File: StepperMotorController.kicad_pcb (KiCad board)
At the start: 4 copper layers, 80 x 100 mm, 66 parts, among them J1 Conn_01x04, J2 Conn_01x04, J3 Conn_01x08, J4 Conn_01x02, J5 TC2070, M1 Mounting_Hole, M2 Mounting_Hole, M3 Mounting_Hole, M4 Mounting_Hole, U1 ACS725xLCTR-10AU, U10 SIR5802DP, U11 TMC5160A-TA, U12 STM32U575RGTx, U13 MCP2562-H-SN, U14 AP62300TWU, U2 AP62300TWU, U3 SIR5802DP, U4 SIR5802DP, U5 SIR5802DP, U6 SIR5802DP, U7 SIR5802DP, U8 SIR5802DP, U9 SIR5802DP

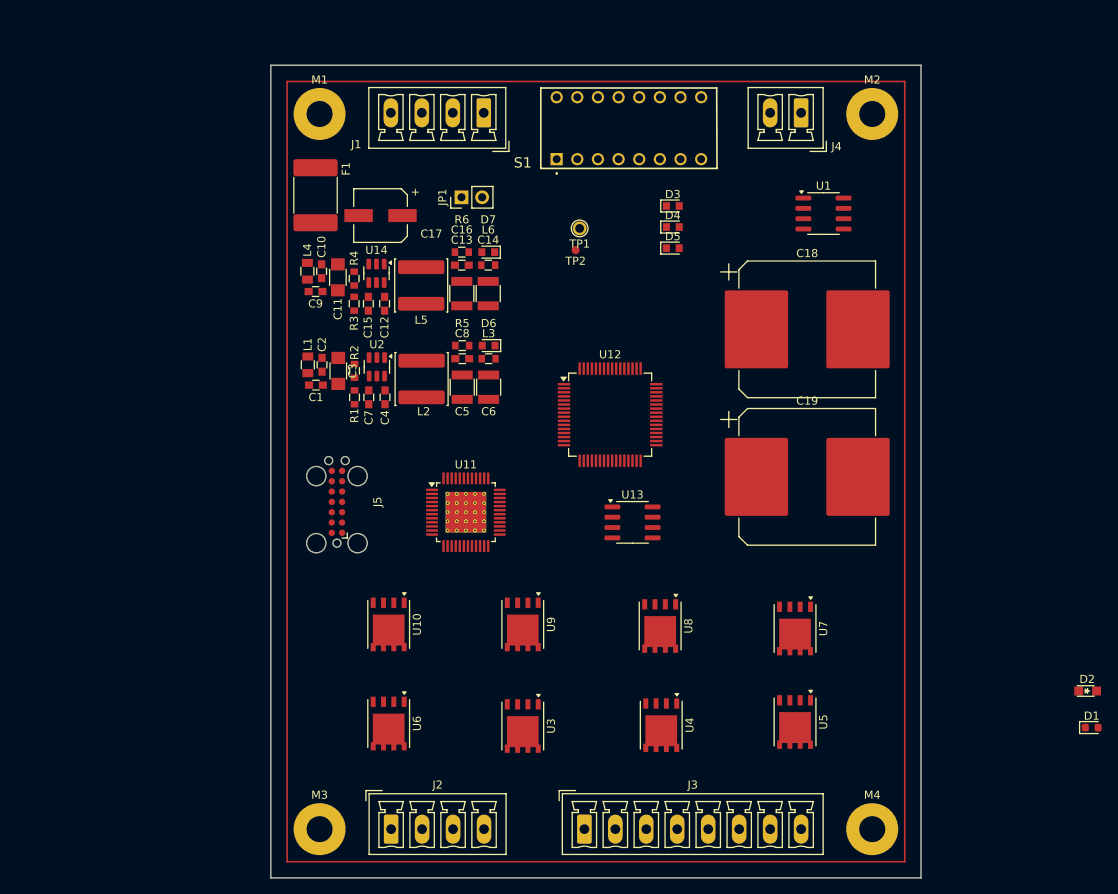
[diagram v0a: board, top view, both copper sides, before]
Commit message: PCB 3mm free space around edges, 9pin dipswitch, re-arragnged components
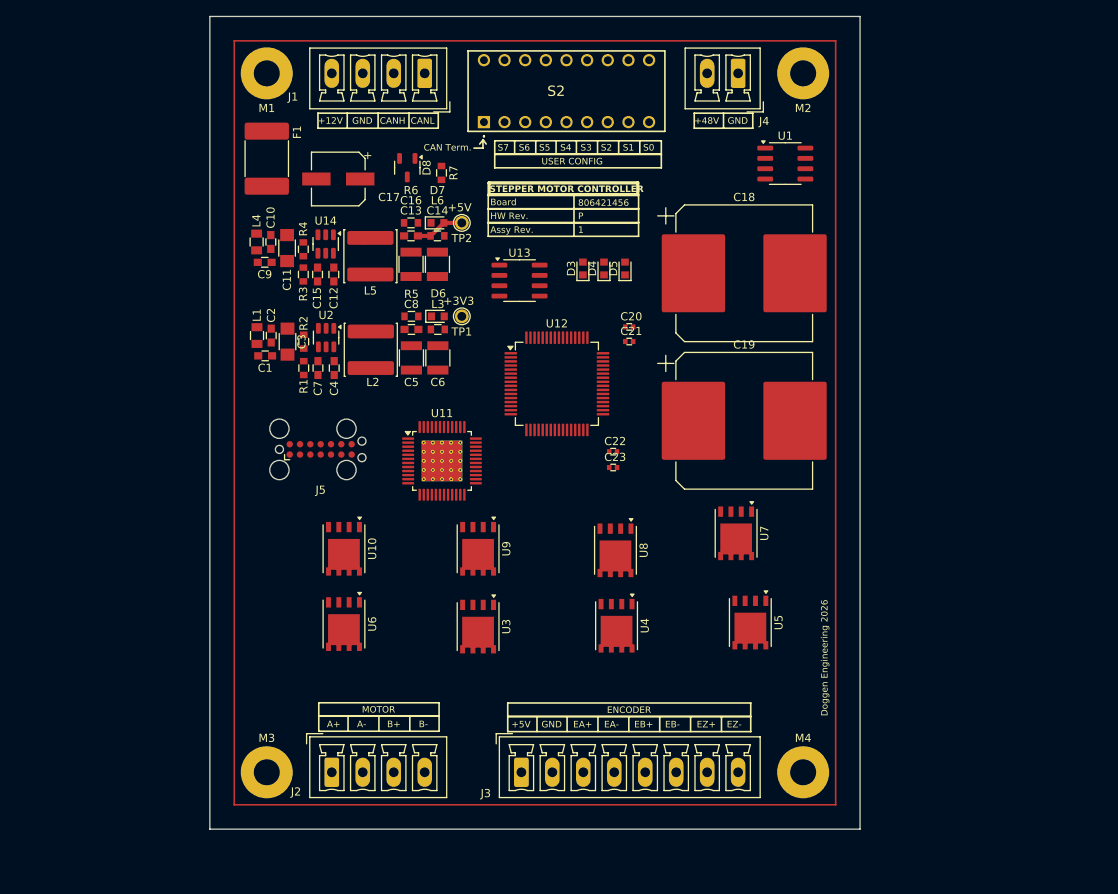
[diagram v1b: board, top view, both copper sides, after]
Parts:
- removed D1: LED, LED_SMD:LED_0603_1608Metric
- removed D2: LED0805BLUE#0805LED, D&R_Discrete:LED_0805
- removed JP1: Jumper_2_Open, Connector_PinHeader_2.54mm:PinHeader_1x02_P2.54mm_Vertical
- removed S1: MCNDS-08V, Doggen:MCNDS08V
- added C20: 100N-X7R_25V#0402, D&R_Passive:C_0402, F.Cu at (131.6, 58.2)
- added C21: 100N-X7R_25V#0402, D&R_Passive:C_0402, F.Cu at (131.6, 60.0)
- added C22: 100N-X7R_25V#0402, D&R_Passive:C_0402, F.Cu at (129.6, 73.5)
- added C23: 100N-X7R_25V#0402, D&R_Passive:C_0402, F.Cu at (129.6, 75.5)
- added D8: TPSM24CANB-02HTG, Package_TO_SOT_SMD:SOT-23-3, F.Cu at (104.3, 38.6)
- added R7: 120R#0603, D&R_Passive:R_0603, F.Cu at (108.5, 39.2)
- added S2: MCNDS-09V, Doggen:MCNDS09V, F.Cu at (113.7, 33.0)
- TP2: value Testpin -> Testpin_via; footprint D&R_Other:TP1mm -> D&R_Other:Testpoint_Via
- moved U13 32.8 mm to (118.1, 52.5)
- moved TP1 18.1 mm to (111.0, 56.9)
- moved TP2 14.4 mm to (111.0, 45.4)
- moved U7 13.8 mm to (144.8, 83.6)
- moved D3 13.5 mm to (125.9, 51.0), turned to 90 degrees
- moved U3 13.4 mm to (113.0, 95.1)
- moved U4 13.4 mm to (130.0, 95.0)
- moved U5 13.4 mm to (146.5, 94.6)
- moved U6 13.4 mm to (96.5, 94.8)
- moved M4 11.0 mm to (153.0, 113.0)
- moved U10 10.8 mm to (96.5, 85.5)
- moved U8 10.8 mm to (129.9, 85.7)
- moved U9 10.8 mm to (113.0, 85.5)
- moved J3 10.4 mm to (118.3, 113.0)
- moved C19 10.4 mm to (145.8, 69.8)
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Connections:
- J1 pad 1: GND -> Net-(J1-Pin_1)
- J1 pad 2: +12V -> Net-(J1-Pin_2)
- J1 pad 3: unconnected-(J1-Pin_3-Pad3) -> GND
- J1 pad 4: unconnected-(J1-Pin_4-Pad4) -> +12V
- TP1 pad 1: unconnected-(TP1-Pad1) -> +3V3
- TP2 pad 1: unconnected-(TP2-Pad1) -> +5V
- U12 pad 19: unconnected-(U12-VDD-Pad19) -> +3V3
- U12 pad 32: unconnected-(U12-VDD-Pad32) -> +3V3
- U12 pad 64: unconnected-(U12-VDD-Pad64) -> +3V3
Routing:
- net +5V: track 0.00 -> 6.06 mm
- net Net-(U14-SW): track 0.00 -> 1.06 mm
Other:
- board text added: "+12V"
- board text added: "+3V3"
- board text added: "+48V"
- board text added: "+5V"
- board text added: "1"
- board text added: "806421456"
- board text added: "A+"
- board text added: "A-"
- board text added: "Assy Rev."
- board text added: "B+"
- board text added: "B-"
- board text added: "Board"
- board text added: "CAN Term."
- board text added: "CANH"
- board text added: "CANL"
- board text added: "Doggen Engineering 2026"
- board text added: "EA+"
- board text added: "EA-"
- board text added: "EB+"
- board text added: "EB-"
- board text added: "ENCODER"
- board text added: "EZ+"
- board text added: "EZ-"
- board text added: "GND"
- board text added: "HW Rev."
- board text added: "MOTOR"
- board text added: "P"
- board text added: "S0"
- board text added: "S1"
- board text added: "S2"
- board text added: "S3"
- board text added: "S4"
- board text added: "S5"
- board text added: "S6"
- board text added: "S7"
- board text added: "STEPPER MOTOR CONTROLLER"
- board text added: "USER CONFIG"

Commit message: updated hierarchical sheets
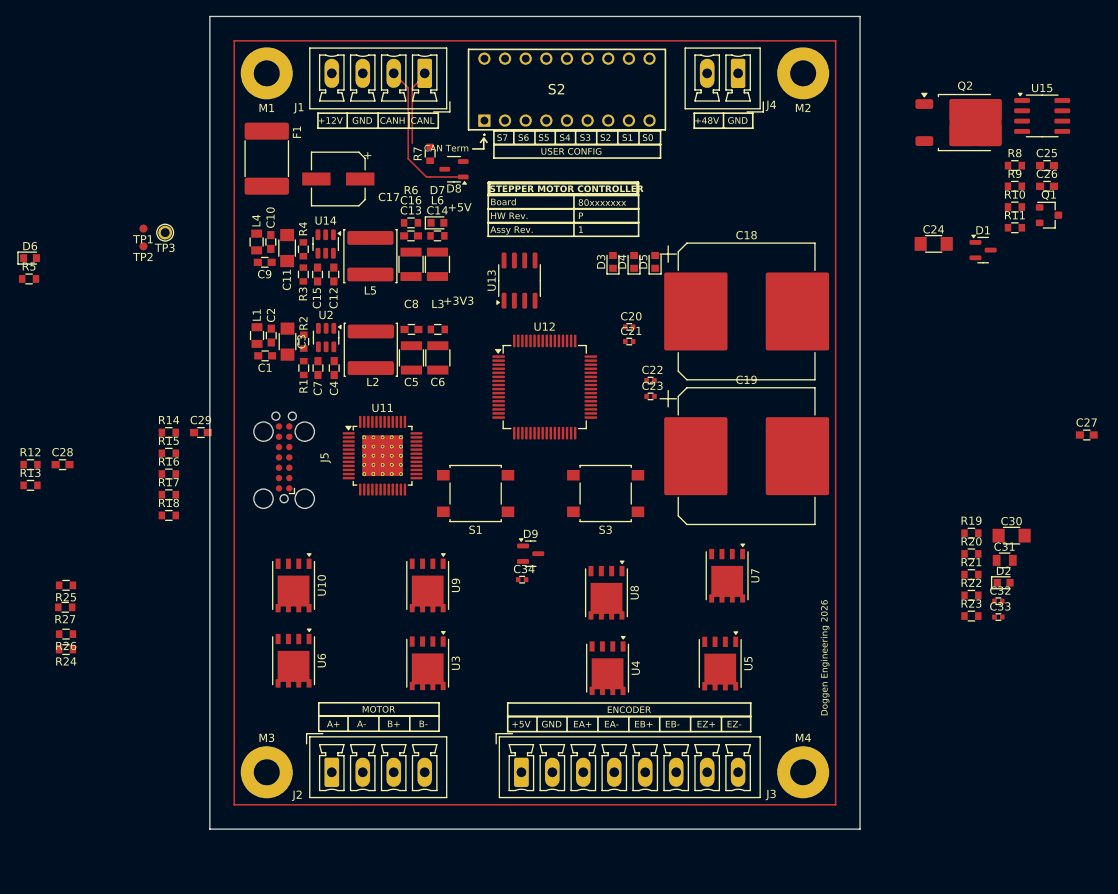
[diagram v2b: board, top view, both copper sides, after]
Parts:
- removed U1: ACS725xLCTR-10AU, Package_SO:SOIC-8_3.9x4.9mm_P1.27mm
- added C24: 10U-X5R_50V#1206, D&R_Passive:C_1206, F.Cu at (169.1, 48.0)
- added C25: 100N-X7R_50V#0603, D&R_Passive:C_0603, F.Cu at (183.0, 38.4)
- added C26: 1N-NP0_100V#0603, D&R_Passive:C_0603, F.Cu at (183.0, 40.9)
- added C27: 100N-X7R_100V#0603, D&R_Passive:C_0603, F.Cu at (187.9, 71.5)
- added C28: 100N-X7R_50V#0603, D&R_Passive:C_0603, F.Cu at (61.9, 75.2)
- added C29: 33P-NP0_50V#0603, D&R_Passive:C_0603, F.Cu at (78.9, 71.2)
- added C30: 4U7-X7R_25V#1206, D&R_Passive:C_1206, F.Cu at (178.7, 83.9)
- added C31: 1U-X7R_10V#0805, D&R_Passive:C_0805, F.Cu at (177.8, 86.9)
- added C32: 100N-X7R_25V#0402, D&R_Passive:C_0402, F.Cu at (177.0, 92.0)
- added C33: 100N-X7R_25V#0402, D&R_Passive:C_0402, F.Cu at (177.0, 93.9)
- added C34: 100N-X7R_25V#0402, D&R_Passive:C_0402, F.Cu at (118.4, 89.3)
- added D1: BZX84C15, Package_TO_SOT_SMD:SOT-23, F.Cu at (175.1, 48.8)
- added D2: LED0603BLUE_APT1608LVBC/D, D&R_Discrete:LED_0603_1608Metric, F.Cu at (177.7, 89.7)
- added D9: BAT54C, Package_TO_SOT_SMD:SOT-23, F.Cu at (119.5, 86.1)
- added Q1: BC807-25LT1#SOT23, D&R_Discrete:SOT-23, F.Cu at (183.2, 44.5)
- added Q2: MDT40P10D, Package_TO_SOT_SMD:TO-252-2, F.Cu at (172.9, 33.1)
- added R10: 56K#0603, D&R_Passive:R_0603, F.Cu at (179.1, 43.5)
- added R11: 1K#0603, D&R_Passive:R_0603, F.Cu at (179.1, 46.0)
- added R12: 10K#0603, D&R_Passive:R_0603, F.Cu at (57.9, 75.2)
- added R13: 10K#0603, D&R_Passive:R_0603, F.Cu at (57.9, 77.7)
- added R14: 100R#0603, D&R_Passive:R_0603, F.Cu at (75.0, 71.2)
- added R15: 100R#0603, D&R_Passive:R_0603, F.Cu at (75.0, 73.8)
- added R16: 100R#0603, D&R_Passive:R_0603, F.Cu at (75.0, 76.3)
- added R17: 10K#0603, D&R_Passive:R_0603, F.Cu at (75.0, 78.8)
- added R18: 100R#0603, D&R_Passive:R_0603, F.Cu at (75.0, 81.4)
- added R19: 3K3#0603, D&R_Passive:R_0603, F.Cu at (173.7, 83.6)
- added R20: 3K3#0603, D&R_Passive:R_0603, F.Cu at (173.7, 86.1)
- added R21: 3K3#0603, D&R_Passive:R_0603, F.Cu at (173.7, 88.7)
- added R22: 1K#0603, D&R_Passive:R_0603, F.Cu at (173.7, 91.2)
- added R23: 10R#0603, D&R_Passive:R_0603, F.Cu at (173.7, 93.8)
- added R24: 47R#0603, D&R_Passive:R_0603, F.Cu at (62.3, 97.9)
- added R25: 47R#0603, D&R_Passive:R_0603, F.Cu at (62.3, 90.0)
- added R26: 47R#0603, D&R_Passive:R_0603, F.Cu at (62.3, 96.0)
- added R27: 47R#0603, D&R_Passive:R_0603, F.Cu at (62.2, 92.7)
- added R8: 100R#0603, D&R_Passive:R_0603, F.Cu at (179.1, 38.4)
- added R9: 100K#0603, D&R_Passive:R_0603, F.Cu at (179.1, 40.9)
- added S1: Wurth_Tactile_Switch_430182043816, Button_Switch_SMD:SW_SPST_B3S-1000, F.Cu at (112.7, 78.7)
- added S3: Wurth_Tactile_Switch_430182043816, Button_Switch_SMD:SW_SPST_B3S-1000, F.Cu at (128.7, 78.7)
- added TP3: Testpin_via, D&R_Other:Testpoint_Via, F.Cu at (74.5, 46.6)
- added U15: ACS725xLCTR-30AB, Package_SO:SOIC-8_3.9x4.9mm_P1.27mm, F.Cu at (182.4, 32.2)
- TP1, TP2: value Testpin_via -> Testpin; footprint D&R_Other:Testpoint_Via -> D&R_Other:TP1mm
- moved D6 50.7 mm to (57.9, 49.7)
- moved R5 47.3 mm to (57.8, 52.3), turned to 0 degrees
- moved TP1 40.6 mm to (71.8, 46.1)
- moved TP2 39.3 mm to (71.8, 48.3)
- moved C22 9.89 mm to (134.2, 64.8)
- moved C23 9.89 mm to (134.2, 66.8)
- moved U10 7.67 mm to (90.3, 90.0)
- moved U6 7.67 mm to (90.3, 99.3)
- moved U9 7.67 mm to (106.8, 90.0)
- moved U3 7.67 mm to (106.8, 99.6)
- moved U11 7.34 mm to (101.2, 74.0)
- moved U5 6.26 mm to (142.8, 99.6)
- moved D8 5.75 mm to (110.0, 38.8), turned to 180 degrees
- moved U4 5.34 mm to (128.9, 100.2)
- moved U7 5.34 mm to (143.6, 88.8)
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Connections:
- C1 pad 2: Net-(C1-Pad2) -> +12V
- C17 pad 1: Net-(C1-Pad2) -> +12V
- C18 pad 1: unconnected-(C18-Pad1) -> +48V
- C18 pad 2: unconnected-(C18-Pad2) -> GND
- C19 pad 1: unconnected-(C19-Pad1) -> +48V
- C19 pad 2: unconnected-(C19-Pad2) -> GND
- C9 pad 2: Net-(C1-Pad2) -> +12V
- D3 pad 1: unconnected-(D3-K-Pad1) -> Net-(D3-K)
- D3 pad 2: unconnected-(D3-A-Pad2) -> /STM32U575RGTx/LED_RED
- D4 pad 1: unconnected-(D4-K-Pad1) -> Net-(D4-K)
- D4 pad 2: unconnected-(D4-A-Pad2) -> /STM32U575RGTx/LED_GRN
- D5 pad 1: unconnected-(D5-K-Pad1) -> Net-(D5-K)
- D5 pad 2: unconnected-(D5-A-Pad2) -> /STM32U575RGTx/LED_ORANGE
- D8 pad 1: Net-(J1-Pin_1) -> CANH
- D8 pad 2: Net-(J1-Pin_2) -> CANL
- F1 pad 1: +12V -> Net-(J1-Pin_4)
- F1 pad 2: Net-(C1-Pad2) -> +12V
- J1 pad 1: Net-(J1-Pin_1) -> CANL
- J1 pad 2: Net-(J1-Pin_2) -> CANH
- J1 pad 4: +12V -> Net-(J1-Pin_4)
- J4 pad 1: unconnected-(J4-Pin_1-Pad1) -> GND
- J4 pad 2: unconnected-(J4-Pin_2-Pad2) -> /PSU/+48V_IN
- J5 pad 1: unconnected-(J5-Pad1) -> Net-(J5-Pad1)
- J5 pad 10: unconnected-(J5-Pad10) -> GND
- J5 pad 11: unconnected-(J5-Pad11) -> /STM32U575RGTx/USART2_RX
- J5 pad 12: unconnected-(J5-Pad12) -> /STM32U575RGTx/USART2_TX
- J5 pad 2: unconnected-(J5-Pad2) -> /STM32U575RGTx/NRESET
- J5 pad 3: unconnected-(J5-Pad3) -> /STM32U575RGTx/TDI
- J5 pad 5: unconnected-(J5-Pad5) -> +3V3
- J5 pad 6: unconnected-(J5-Pad6) -> GND
- J5 pad 7: unconnected-(J5-Pad7) -> Net-(J5-Pad7)
- J5 pad 9: unconnected-(J5-Pad9) -> Net-(J5-Pad9)
- L1 pad 1: Net-(C1-Pad2) -> +12V
- L4 pad 1: Net-(C1-Pad2) -> +12V
- R7 pad 1: Net-(S2-COM_1) -> CANH
- R7 pad 2: Net-(J1-Pin_2) -> Net-(S2-NO_1)
- S2 pad A1: Net-(S2-COM_1) -> CANL
- S2 pad A2: unconnected-(S2-COM_2-PadA2) -> /STM32U575RGTx/S7
- S2 pad A3: unconnected-(S2-COM_3-PadA3) -> /STM32U575RGTx/S6
- S2 pad A4: unconnected-(S2-COM_4-PadA4) -> /STM32U575RGTx/S5
- S2 pad A5: unconnected-(S2-COM_5-PadA5) -> /STM32U575RGTx/S4
- S2 pad A6: unconnected-(S2-COM_6-PadA6) -> /STM32U575RGTx/S3
- S2 pad A7: unconnected-(S2-COM_7-PadA7) -> /STM32U575RGTx/S2
- S2 pad A8: unconnected-(S2-COM_8-PadA8) -> /STM32U575RGTx/S1
- S2 pad A9: unconnected-(S2-COM_9-PadA9) -> /STM32U575RGTx/S0
- S2 pad B1: Net-(J1-Pin_1) -> Net-(S2-NO_1)
- S2 pad B2: unconnected-(S2-NO_2-PadB2) -> GND
- S2 pad B3: unconnected-(S2-NO_3-PadB3) -> GND
- S2 pad B4: unconnected-(S2-NO_4-PadB4) -> GND
- S2 pad B5: unconnected-(S2-NO_5-PadB5) -> GND
- S2 pad B6: unconnected-(S2-NO_6-PadB6) -> GND
- S2 pad B7: unconnected-(S2-NO_7-PadB7) -> GND
- S2 pad B8: unconnected-(S2-NO_8-PadB8) -> GND
- S2 pad B9: unconnected-(S2-NO_9-PadB9) -> GND
- U11 pad 13: /TMC5160/CS -> /STM32U575RGTx/~{TMC5160_CS}
- U11 pad 14: /TMC5160/SCLK -> /STM32U575RGTx/TMC5160_SCLK
- U11 pad 15: /TMC5160/MOSI -> /STM32U575RGTx/TMC5160_MOSI
- U11 pad 16: /TMC5160/MISO -> Net-(U11-SDO/CFG0)
- U12 pad 1: unconnected-(U12-VBAT-Pad1) -> +3V3
- U12 pad 12: unconnected-(U12-VSSA-Pad12) -> GND
- U12 pad 13: unconnected-(U12-VDDA-Pad13) -> Net-(U12-VDDA)
- U12 pad 15: unconnected-(U12-PA1-Pad15) -> Net-(U12-PA1)
- U12 pad 16: unconnected-(U12-PA2-Pad16) -> /STM32U575RGTx/USART2_TX
- U12 pad 17: unconnected-(U12-PA3-Pad17) -> /STM32U575RGTx/USART2_RX
- U12 pad 18: Net-(U12-VSS-Pad18) -> GND
- U12 pad 20: unconnected-(U12-PA4-Pad20) -> Net-(U12-PA4)
- U12 pad 22: unconnected-(U12-PA6-Pad22) -> /STM32U575RGTx/TMC5160_MISO
- U12 pad 23: unconnected-(U12-PA7-Pad23) -> Net-(U12-PA7)
- U12 pad 30: unconnected-(U12-VCAP-Pad30) -> Net-(U12-VCAP)
- U12 pad 31: Net-(U12-VSS-Pad18) -> GND
- U12 pad 46: unconnected-(U12-PA13-Pad46) -> /STM32U575RGTx/TMS
- U12 pad 47: Net-(U12-VSS-Pad18) -> GND
- U12 pad 48: unconnected-(U12-VDDUSB-Pad48) -> +3V3
- U12 pad 49: unconnected-(U12-PA14-Pad49) -> /STM32U575RGTx/TCK
- U12 pad 50: unconnected-(U12-PA15-Pad50) -> /STM32U575RGTx/TDI
- U12 pad 55: unconnected-(U12-PB3-Pad55) -> /STM32U575RGTx/TDO
- U12 pad 56: unconnected-(U12-PB4-Pad56) -> /STM32U575RGTx/NRESET
- U12 pad 60: unconnected-(U12-PH3-Pad60) -> Net-(U12-PH3)
- U12 pad 61: unconnected-(U12-PB8-Pad61) -> /STM32U575RGTx/CAN_RX
- U12 pad 62: unconnected-(U12-PB9-Pad62) -> /STM32U575RGTx/CAN_TX
- U12 pad 63: Net-(U12-VSS-Pad18) -> GND
- U12 pad 7: unconnected-(U12-NRST-Pad7) -> Net-(U12-NRST)
- U13 pad 1: unconnected-(U13-TXD-Pad1) -> /STM32U575RGTx/CAN_RX
- U13 pad 2: unconnected-(U13-VSS-Pad2) -> GND
- U13 pad 3: unconnected-(U13-VDD-Pad3) -> +3V3
- U13 pad 4: unconnected-(U13-RXD-Pad4) -> /STM32U575RGTx/CAN_TX
- U13 pad 5: unconnected-(U13-Vio-Pad5) -> +3V3
- U13 pad 6: unconnected-(U13-CANL-Pad6) -> CANL
- U13 pad 7: unconnected-(U13-CANH-Pad7) -> CANH
- U13 pad 8: unconnected-(U13-STBY-Pad8) -> GND
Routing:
- net CANH: track 0.00 -> 19.3 mm
- net CANL: track 0.00 -> 9.37 mm
- net +5V: track 6.06 -> 0.04 mm
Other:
- board text added: "80xxxxxxx"
- board text added: "CAN Term"
- board text removed: "806421456"
- board text removed: "CAN Term."

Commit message: PCB Finished, only have to check LED's
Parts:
- removed the C33 at (177.0, 93.9)
- removed the TP3 at (74.5, 46.6)
- removed the U4 at (128.9, 100.2)
- removed the U5 at (142.8, 99.6)
- removed U7, U8: SIR5802DP, Package_SO:PowerPAK_SO-8_Single
- added C34: 100N-X7R_25V#0402, D&R_Passive:C_0402, F.Cu at (118.5, 54.5)
- added C35: 470N-X7R_50V#0805, D&R_Passive:C_0805, F.Cu at (127.0, 79.9)
- added C36: 470N-X7R_50V#0805, D&R_Passive:C_0805, F.Cu at (124.4, 83.5)
- added C37: 470N-X7R_100V#1210, D&R_Passive:C_1210, F.Cu at (164.6, 97.4)
- added C38: 100N-X7R_100V#0603, D&R_Passive:C_0603, F.Cu at (135.0, 78.2)
- added C39: 2U2-X5R_25V#0603, D&R_Passive:C_0603, F.Cu at (129.8, 76.3)
- added C40: 2U2-X5R_25V#0603, D&R_Passive:C_0603, F.Cu at (128.9, 79.9)
- added C41: 470N-X7R_50V#0805, D&R_Passive:C_0805, F.Cu at (113.8, 70.2)
- added C42: 100N-X7R_25V#0402, D&R_Passive:C_0402, F.Cu at (118.7, 68.2)
- added C43: 22N-X7R_100V#0603, D&R_Passive:C_0603, F.Cu at (113.8, 73.5)
- added C44: 100N-X7R_100V#0603, D&R_Passive:C_0603, F.Cu at (113.8, 76.6)
- added C45: 100N-X7R_100V#0603, D&R_Passive:C_0603, F.Cu at (157.7, 77.4)
- added C46: 470N-X7R_50V#0805, D&R_Passive:C_0805, F.Cu at (122.3, 83.5)
- added C47: 470N-X7R_50V#0805, D&R_Passive:C_0805, F.Cu at (117.9, 79.9)
- added C48: 470N-X7R_100V#1210, D&R_Passive:C_1210, F.Cu at (85.4, 97.4)
- added C49: 100N-X7R_50V#0603, D&R_Passive:C_0603, F.Cu at (143.1, 66.8)
- added C50: 100N-X7R_25V#0402, D&R_Passive:C_0402, F.Cu at (118.5, 57.1)
- added C51: 100N-X7R_25V#0402, D&R_Passive:C_0402, F.Cu at (118.5, 59.7)
- added C52: 100N-X7R_25V#0402, D&R_Passive:C_0402, F.Cu at (115.7, 65.3)
- added C53: 100N-X7R_25V#0402, D&R_Passive:C_0402, F.Cu at (113.1, 65.3)
- added C54: 100N-X7R_25V#0402, D&R_Passive:C_0402, F.Cu at (118.3, 65.3)
- added C55: 100N-X7R_25V#0402, D&R_Passive:C_0402, F.Cu at (134.5, 62.1)
- added C56: 100N-X7R_25V#0402, D&R_Passive:C_0402, F.Cu at (119.0, 51.2)
- added D10: LED0603ORANGE_APT1608SECK, D&R_Discrete:LED_0603_1608Metric, F.Cu at (112.3, 80.4)
- added J6: Conn_01x03, Connector_Phoenix_MC:PhoenixContact_MCV_1,5_3-G-3.81_1x03_P3.81mm_Vertical, F.Cu at (95.0, 113.0)
- added R28: 120R#0603, D&R_Passive:R_0603, F.Cu at (143.2, 74.0)
- added R29: 120R#0603, D&R_Passive:R_0603, F.Cu at (139.7, 74.0)
- added R30: 120R#0603, D&R_Passive:R_0603, F.Cu at (139.7, 66.8)
- added R31: 27R#0805, D&R_Passive:R_0805, F.Cu at (145.8, 97.8)
- added R32: 1K#0603, D&R_Passive:R_0603, F.Cu at (131.3, 39.2)
- added R33: 1K#0603, D&R_Passive:R_0603, F.Cu at (129.5, 39.2)
- added R34: 1K#0603, D&R_Passive:R_0603, F.Cu at (127.7, 39.2)
- added R35: 1K#0603, D&R_Passive:R_0603, F.Cu at (125.9, 39.2)
- added R36: 1K#0603, D&R_Passive:R_0603, F.Cu at (124.1, 39.2)
- added R37: 1K#0603, D&R_Passive:R_0603, F.Cu at (122.3, 39.2)
- added R38: 1K#0603, D&R_Passive:R_0603, F.Cu at (120.5, 39.2)
- added R39: 1K#0603, D&R_Passive:R_0603, F.Cu at (118.7, 39.2)
- added R40: 27R#0805, D&R_Passive:R_0805, F.Cu at (145.8, 85.8)
- added R41: 2R2#0603, D&R_Passive:R_0603, F.Cu at (131.4, 76.3)
- added R42: 27R#0805, D&R_Passive:R_0805, F.Cu at (111.8, 97.8)
- added R43: 27R#0805, D&R_Passive:R_0805, F.Cu at (128.8, 97.8)
- added R44: 27R#0805, D&R_Passive:R_0805, F.Cu at (128.8, 85.8)
- added R45: 27R#0805, D&R_Passive:R_0805, F.Cu at (111.8, 85.8)
- added R46: 27R#0805, D&R_Passive:R_0805, F.Cu at (94.8, 97.8)
- added R47: 47R#0603, D&R_Passive:R_0603, F.Cu at (135.0, 68.1)
- added R48: 47R#0603, D&R_Passive:R_0603, F.Cu at (164.0, 85.1)
- added R49: 47R#0603, D&R_Passive:R_0603, F.Cu at (166.0, 85.1)
- added R50: 47R#0603, D&R_Passive:R_0603, F.Cu at (85.9, 85.1)
- added R51: 47R#0603, D&R_Passive:R_0603, F.Cu at (83.9, 85.1)
- added R52: 47R#0603, D&R_Passive:R_0603, F.Cu at (135.0, 71.3)
- added R53: 27R#0805, D&R_Passive:R_0805, F.Cu at (94.8, 85.8)
- added R54: 0R05#2512, D&R_Passive:R_2512, F.Cu at (163.0, 93.7)
- added R55: 0R05#2512, D&R_Passive:R_2512, F.Cu at (163.0, 89.2)
- added R56: 0R05#2512, D&R_Passive:R_2512, F.Cu at (87.0, 93.7)
- added R57: 0R05#2512, D&R_Passive:R_2512, F.Cu at (87.0, 89.2)
- added R58: 47R#0603, D&R_Passive:R_0603, F.Cu at (135.0, 74.5)
- added R59: 47R#0603, D&R_Passive:R_0603, F.Cu at (135.0, 69.7)
- added R60: 47R#0603, D&R_Passive:R_0603, F.Cu at (135.0, 72.9)
- added R61: 47R#0603, D&R_Passive:R_0603, F.Cu at (135.0, 76.1)
- added R62: 10K#0603, D&R_Passive:R_0603, F.Cu at (142.3, 60.6)
- added R63: 10K#0603, D&R_Passive:R_0603, F.Cu at (87.6, 54.0)
- added R64: 10K#0603, D&R_Passive:R_0603, F.Cu at (115.7, 57.5)
- added R65: 150K#0603, D&R_Passive:R_0603, F.Cu at (143.9, 60.6)
- added R66: 33K#0603, D&R_Passive:R_0603, F.Cu at (86.0, 54.0)
- added R67: 10K#0603, D&R_Passive:R_0603, F.Cu at (114.1, 57.5)
- added R68: 1K#0603, D&R_Passive:R_0603, F.Cu at (118.0, 53.2)
- added R69: 1K#0603, D&R_Passive:R_0603, F.Cu at (118.0, 55.8)
- added R70: 1K#0603, D&R_Passive:R_0603, F.Cu at (118.0, 58.4)
- added R71: 33K#0603, D&R_Passive:R_0603, F.Cu at (114.4, 62.0)
- added R72: 10K#0603, D&R_Passive:R_0603, F.Cu at (114.4, 65.0)
- added R73: 1K#0603, D&R_Passive:R_0603, F.Cu at (134.0, 63.4)
- added R74: 10K#0603, D&R_Passive:R_0603, F.Cu at (111.8, 62.0)
- added R75: 10K#0603, D&R_Passive:R_0603, F.Cu at (111.8, 65.0)
- added R76: 10K#0603, D&R_Passive:R_0603, F.Cu at (117.0, 62.0)
- added R77: 10K#0603, D&R_Passive:R_0603, F.Cu at (117.0, 65.0)
- added R78: 3K3#0603, D&R_Passive:R_0603, F.Cu at (102.4, 80.4)
- added R79: 3K3#0603, D&R_Passive:R_0603, F.Cu at (109.3, 80.4)
- added R80: 33K#0603, D&R_Passive:R_0603, F.Cu at (91.9, 55.8)
- added R81: 10K#0603, D&R_Passive:R_0603, F.Cu at (93.6, 55.8)
- added R82: 1K#0603, D&R_Passive:R_0603, F.Cu at (95.2, 55.8)
- added U15: SIR5802DP, Package_SO:PowerPAK_SO-8_Single, F.Cu at (116.5, 100.5)
- added U16: AM26LV32E, Package_SO:TSSOP-16_4.4x5mm_P0.65mm, F.Cu at (140.8, 70.4)
- added U17: SIR5802DP, Package_SO:PowerPAK_SO-8_Single, F.Cu at (116.5, 88.5)
- added U18: SIR5802DP, Package_SO:PowerPAK_SO-8_Single, F.Cu at (99.5, 100.5)
- added U6: SIR5802DP, Package_SO:PowerPAK_SO-8_Single, F.Cu at (99.5, 88.5)
- D9: value BAT54C -> LED0603GRN_APT1608ZGC; footprint Package_TO_SOT_SMD:SOT-23 -> D&R_Discrete:LED_0603_1608Metric
- U4: renamed from U11; footprint Package_QFP:TQFP-48-1EP_7x7mm_P0.5mm_EP5x5mm_ThermalVias -> Package_QFP:TQFP-48-1EP_7x7mm_P0.5mm_EP5x5mm
- moved R20 74.6 mm to (130.5, 65.7), turned to -90 degrees
- moved R11 71.1 mm to (125.7, 65.7), turned to -90 degrees
- moved R16 70.9 mm to (128.9, 65.7), turned to -90 degrees
- moved R23 70.5 mm to (127.3, 65.7), turned to -90 degrees
- moved R13 66.1 mm to (137.0, 51.1), turned to -90 degrees
- moved R15 65.1 mm to (132.2, 45.3), turned to 90 degrees
- moved R12 62.1 mm to (120.3, 62.0), turned to 90 degrees
- moved U11 61.2 mm to (150.5, 88.5)
- moved U12 61.1 mm to (150.5, 100.5)
- moved C24 61.0 mm to (122.1, 62.1), turned to -90 degrees
- moved R17 59.8 mm to (128.8, 45.3), turned to -90 degrees
- moved C33 59.4 mm to (134.8, 50.1)
- moved R26 59.4 mm to (137.1, 41.9), turned to -90 degrees
- moved R27 59.2 mm to (140.9, 41.9), turned to 90 degrees
- moved R25 58.7 mm to (135.1, 41.9), turned to -90 degrees
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- renumbered C17 to C1, C12 to C10, C9 to C11, C10 to C12, C11 to C13, C13 to C14, C14 to C15, C15 to C16, C16 to C17, C24 to C18, C18 to C19, C4 to C2, C19 to C20, C27 to C21, C25 to C22, C26 to C23, C31 to C24, C28 to C25, C34 to C26, C29 to C27, C30 to C28, C20 to C29, C1 to C3, C21 to C30, C22 to C31, C23 to C32, C32 to C33, C2 to C4, C3 to C5, C5 to C6, C6 to C7, C7 to C8, C8 to C9, D7 to D1, D6 to D2, D1 to D3, D8 to D4, D3 to D5, D4 to D6, D5 to D7, D2 to D8, J4 to J2, J2 to J3, J3 to J4, Q2 to Q1, Q1 to Q2, R6 to R1, R11 to R10, R24 to R11, R23 to R12, R15 to R13, R12 to R14, R16 to R15, R25 to R16, R14 to R17, R7 to R19, R5 to R2, R26 to R20, R17 to R21, R13 to R22, R27 to R23, R19 to R24, R20 to R25, R21 to R26, R22 to R27, R1 to R3, R2 to R4, R3 to R5, R4 to R6, R10 to R7, S3 to S2, S2 to S3, TP1 to TP2, TP2 to TP3, U2 to U1, U9 to U10, U6 to U11, U10 to U12, U12 to U14, U14 to U2, U15 to U3, U3 to U5
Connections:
- net Net-(C13-Pad1) renamed /PSU/5V_OUT
- net Net-(Q2-D) renamed /PSU/FET_OUT
- net Net-(U14-IN) renamed /PSU/5V_REG_IN
- net Net-(U14-SW) renamed /PSU/5V_REG_OUT
- D9 pad 1: unconnected-(D9-Pad1) -> Net-(D9-K)
- D9 pad 2: unconnected-(D9-Pad2) -> /TMC5160/DIR_OUT
- J1 pad 1: CANL -> GND
- J1 pad 2: CANH -> CANL
- J1 pad 3: GND -> CANH
- J3 pad 1: unconnected-(J2-Pin_1-Pad1) -> /TMC5160/BMA2
- J3 pad 2: unconnected-(J2-Pin_2-Pad2) -> /TMC5160/BMA1
- J3 pad 3: unconnected-(J2-Pin_3-Pad3) -> /TMC5160/BMB2
- J3 pad 4: unconnected-(J2-Pin_4-Pad4) -> /TMC5160/BMB1
- J4 pad 1: unconnected-(J3-Pin_1-Pad1) -> GND
- J4 pad 2: unconnected-(J3-Pin_2-Pad2) -> /Encoder/EA+
- J4 pad 3: unconnected-(J3-Pin_3-Pad3) -> /Encoder/EA-
- J4 pad 4: unconnected-(J3-Pin_4-Pad4) -> /Encoder/EB+
- J4 pad 5: unconnected-(J3-Pin_5-Pad5) -> /Encoder/EB-
- J4 pad 6: unconnected-(J3-Pin_6-Pad6) -> /Encoder/EZ+
- J4 pad 7: unconnected-(J3-Pin_7-Pad7) -> /Encoder/EZ-
- J4 pad 8: unconnected-(J3-Pin_8-Pad8) -> +5V
- M1 pad 1: unconnected-(M1-Pad1) -> GND
- M2 pad 1: unconnected-(M2-Pad1) -> GND
- M3 pad 1: unconnected-(M3-Pad1) -> GND
- M4 pad 1: unconnected-(M4-Pad1) -> GND
- R16 pad 1: Net-(U12-PA1) -> Net-(U14-PA5)
- R20 pad 1: Net-(U12-PA4) -> Net-(U14-PB0)
- S3 pad A2: /STM32U575RGTx/S7 -> Net-(S3-COM_2)
- S3 pad A3: /STM32U575RGTx/S6 -> Net-(S3-COM_3)
- S3 pad A4: /STM32U575RGTx/S5 -> Net-(S3-COM_4)
- S3 pad A5: /STM32U575RGTx/S4 -> Net-(S3-COM_5)
- S3 pad A6: /STM32U575RGTx/S3 -> Net-(S3-COM_6)
- S3 pad A7: /STM32U575RGTx/S2 -> Net-(S3-COM_7)
- S3 pad A8: /STM32U575RGTx/S1 -> Net-(S3-COM_8)
- S3 pad A9: /STM32U575RGTx/S0 -> Net-(S3-COM_9)
- U10 pad 1: unconnected-(U9-S-Pad1) -> /TMC5160/BMB2
- U10 pad 2: unconnected-(U9-S-Pad2) -> /TMC5160/BMB2
- U10 pad 3: unconnected-(U9-S-Pad3) -> /TMC5160/BMB2
- U10 pad 4: unconnected-(U9-G-Pad4) -> Net-(U10-G)
- U10 pad 5: unconnected-(U9-D-Pad5) -> +48V
- U11 pad 1: unconnected-(U6-S-Pad1) -> /TMC5160/SRB
- U11 pad 2: unconnected-(U6-S-Pad2) -> /TMC5160/SRB
- U11 pad 3: unconnected-(U6-S-Pad3) -> /TMC5160/SRB
- U11 pad 4: unconnected-(U6-G-Pad4) -> Net-(U11-G)
- U11 pad 5: unconnected-(U6-D-Pad5) -> /TMC5160/BMB1
- U12 pad 1: unconnected-(U10-S-Pad1) -> /TMC5160/BMB1
- U12 pad 2: unconnected-(U10-S-Pad2) -> /TMC5160/BMB1
- U12 pad 3: unconnected-(U10-S-Pad3) -> /TMC5160/BMB1
- U12 pad 4: unconnected-(U10-G-Pad4) -> Net-(U12-G)
- U12 pad 5: unconnected-(U10-D-Pad5) -> +48V
- U14 pad 10: unconnected-(U12-PC2-Pad10) -> /STM32U575RGTx/ADC4_IN3_5V
- U14 pad 11: unconnected-(U12-PC3-Pad11) -> /STM32U575RGTx/ADC4_IN4_BOARD
- U14 pad 14: unconnected-(U12-PA0-Pad14) -> /STM32U575RGTx/REFL_OUT
- U14 pad 15: Net-(U12-PA1) -> /STM32U575RGTx/REFR_OUT
- U14 pad 2: unconnected-(U12-PC13-Pad2) -> /STM32U575RGTx/S7
- U14 pad 20: Net-(U12-PA4) -> unconnected-(U14-PA4-Pad20)
- U14 pad 21: unconnected-(U12-PA5-Pad21) -> Net-(U14-PA5)
- U14 pad 24: unconnected-(U12-PC4-Pad24) -> /STM32U575RGTx/ADC4_IN22_REV
- U14 pad 25: unconnected-(U12-PC5-Pad25) -> /STM32U575RGTx/ADC4_IN23_ASSY
- U14 pad 26: unconnected-(U12-PB0-Pad26) -> Net-(U14-PB0)
- U14 pad 27: unconnected-(U12-PB1-Pad27) -> Net-(U14-PB1)
- U14 pad 28: unconnected-(U12-PB2-Pad28) -> /STM32U575RGTx/TMC5160_EN
- U14 pad 3: unconnected-(U12-PC14-Pad3) -> /STM32U575RGTx/REF_SW
- U14 pad 38: unconnected-(U12-PC7-Pad38) -> /PSU/48V_EN
- U14 pad 39: unconnected-(U12-PC8-Pad39) -> /STM32U575RGTx/LED_BLUE
- U14 pad 40: unconnected-(U12-PC9-Pad40) -> /STM32U575RGTx/LED_RED
- U14 pad 41: unconnected-(U12-PA8-Pad41) -> /STM32U575RGTx/ENC_A
- U14 pad 42: unconnected-(U12-PA9-Pad42) -> /STM32U575RGTx/ENC_B
- U14 pad 43: unconnected-(U12-PA10-Pad43) -> /STM32U575RGTx/LED_ORANGE
- U14 pad 44: unconnected-(U12-PA11-Pad44) -> /STM32U575RGTx/LED_GRN
- U14 pad 45: unconnected-(U12-PA12-Pad45) -> /STM32U575RGTx/ENC_Z
- U14 pad 51: unconnected-(U12-PC10-Pad51) -> /STM32U575RGTx/S0
- U14 pad 52: unconnected-(U12-PC11-Pad52) -> /STM32U575RGTx/S1
- U14 pad 53: unconnected-(U12-PC12-Pad53) -> /STM32U575RGTx/S2
- U14 pad 54: unconnected-(U12-PD2-Pad54) -> /STM32U575RGTx/S3
- U14 pad 57: unconnected-(U12-PB5-Pad57) -> /STM32U575RGTx/S4
- U14 pad 58: unconnected-(U12-PB6-Pad58) -> /STM32U575RGTx/S5
- U14 pad 59: unconnected-(U12-PB7-Pad59) -> /STM32U575RGTx/S6
- U14 pad 8: unconnected-(U12-PC0-Pad8) -> /STM32U575RGTx/ADC4_IN1_48V
- U14 pad 9: unconnected-(U12-PC1-Pad9) -> /STM32U575RGTx/ADC4_IN2_12V
- U4 pad 1: unconnected-(U11-HB1-Pad1) -> /TMC5160/HB1
- U4 pad 10: unconnected-(U11-SRBL-Pad10) -> /TMC5160/SRBL
- U4 pad 11: unconnected-(U11-TST_MODE-Pad11) -> GND
- U4 pad 12: unconnected-(U11-CLK-Pad12) -> GND
- U4 pad 17: unconnected-(U11-REFL/STEP-Pad17) -> /STM32U575RGTx/REFL_OUT
- U4 pad 18: unconnected-(U11-REFR/DIR-Pad18) -> /STM32U575RGTx/REFR_OUT
- U4 pad 19: Net-(U11-GNDD-Pad19) -> GND
- U4 pad 2: unconnected-(U11-CB1-Pad2) -> /TMC5160/CB1
- U4 pad 20: unconnected-(U11-VCC_IO-Pad20) -> +3V3
- U4 pad 21: unconnected-(U11-SD_MODE-Pad21) -> GND
- U4 pad 22: unconnected-(U11-SPI_MODE-Pad22) -> +3V3
- U4 pad 23: unconnected-(U11-ENCB/DCEN/CFG4-Pad23) -> /TMC5160/ENC_B
- U4 pad 24: unconnected-(U11-ENCA/DCIN/CFG5-Pad24) -> /TMC5160/ENC_A
- U4 pad 25: unconnected-(U11-ENCN/DCO/CFG6-Pad25) -> /TMC5160/ENC_Z
- U4 pad 26: unconnected-(U11-SWN/DIAG0-Pad26) -> /TMC5160/STEP_OUT
- U4 pad 27: unconnected-(U11-SWP/DIAG1-Pad27) -> /TMC5160/DIR_OUT
- U4 pad 28: unconnected-(U11-~{DRV_EN}-Pad28) -> /STM32U575RGTx/TMC5160_EN
- U4 pad 29: unconnected-(U11-VCC-Pad29) -> /TMC5160/VCC
- U4 pad 3: unconnected-(U11-12VOUT-Pad3) -> /TMC5160/12VOUT
- U4 pad 30: Net-(U11-GNDD-Pad19) -> GND
- U4 pad 31: unconnected-(U11-CPO-Pad31) -> /TMC5160/CPO
- U4 pad 32: unconnected-(U11-CPI-Pad32) -> /TMC5160/CPI
- U4 pad 33: unconnected-(U11-VS-Pad33) -> +48V
- U4 pad 34: unconnected-(U11-VCP-Pad34) -> /TMC5160/VCP
- U4 pad 35: unconnected-(U11-CA2-Pad35) -> /TMC5160/CA2
- U4 pad 36: unconnected-(U11-HA2-Pad36) -> /TMC5160/HA2
- U4 pad 37: unconnected-(U11-BMA2-Pad37) -> /TMC5160/BMA2
- U4 pad 38: unconnected-(U11-LA2-Pad38) -> /TMC5160/LA2
- U4 pad 39: unconnected-(U11-LA1-Pad39) -> /TMC5160/LA1
- U4 pad 4: unconnected-(U11-VSA-Pad4) -> +48V
- U4 pad 40: unconnected-(U11-BMA1-Pad40) -> /TMC5160/BMA1
- U4 pad 41: unconnected-(U11-HA1-Pad41) -> /TMC5160/HA1
- U4 pad 42: unconnected-(U11-CA1-Pad42) -> /TMC5160/CA1
- U4 pad 43: unconnected-(U11-CB2-Pad43) -> /TMC5160/CB2
- U4 pad 44: unconnected-(U11-HB2-Pad44) -> /TMC5160/HB2
- U4 pad 45: unconnected-(U11-BMB2-Pad45) -> /TMC5160/BMB2
- U4 pad 46: unconnected-(U11-LB2-Pad46) -> /TMC5160/LB2
- U4 pad 47: unconnected-(U11-LB1-Pad47) -> /TMC5160/LB1
- U4 pad 48: unconnected-(U11-BMB1-Pad48) -> /TMC5160/BMB1
- U4 pad 49: unconnected-(U11-EP-Pad49) -> GND
- U4 pad 5: unconnected-(U11-5VOUT-Pad5) -> /TMC5160/5VOUT
- U4 pad 6: unconnected-(U11-GNDA-Pad6) -> GND
- U4 pad 7: unconnected-(U11-SRAL-Pad7) -> /TMC5160/SRAL
- U4 pad 8: unconnected-(U11-SRAH-Pad8) -> /TMC5160/SRAH
- U4 pad 9: unconnected-(U11-SRBH-Pad9) -> /TMC5160/SRBH
- U5 pad 1: unconnected-(U3-S-Pad1) -> /TMC5160/SRB
- U5 pad 2: unconnected-(U3-S-Pad2) -> /TMC5160/SRB
- U5 pad 3: unconnected-(U3-S-Pad3) -> /TMC5160/SRB
- U5 pad 4: unconnected-(U3-G-Pad4) -> Net-(U5-G)
- U5 pad 5: unconnected-(U3-D-Pad5) -> /TMC5160/BMB2
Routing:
- net +5V: track 0.04 -> 182.6 mm, vias 0 -> 6
- net GND: track 0.00 -> 170.9 mm, vias 0 -> 171
- net +12V: track 0.00 -> 116.9 mm, vias 0 -> 4
- net Net-(J5-Pad7): track 0.00 -> 73.7 mm, vias 0 -> 4
- net Net-(J5-Pad9): track 0.00 -> 73.6 mm, vias 0 -> 2
- net Net-(J6-Pin_2): track 0.00 -> 70.3 mm, vias 0 -> 1
- net Net-(J5-Pad1): track 0.00 -> 64.8 mm, vias 0 -> 2
- net +3V3: track 0.00 -> 62.4 mm, vias 0 -> 24
- net +48V: track 0.00 -> 60.1 mm, vias 0 -> 83
- net /TMC5160/BMB1: track 0.00 -> 59.4 mm, vias 0 -> 53
- net /STM32U575RGTx/TDI: track 0.00 -> 59.1 mm, vias 0 -> 2
- net /Encoder/EA+: track 0.00 -> 57.9 mm, vias 0 -> 1
- net /TMC5160/SRAL: track 0.00 -> 57.1 mm, vias 0 -> 2
- net /STM32U575RGTx/NRESET: track 0.00 -> 56.4 mm, vias 0 -> 2
- net /Encoder/EA-: track 0.00 -> 56.4 mm, vias 0 -> 1
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- added copper zone on In2.Cu, net +3V3
- added copper zone on B.Cu, net +48V
- added copper zone on F.Cu, net +48V
- added copper zone on In2.Cu, net +48V
- added copper zone on F.Cu, net /PSU/+48V_IN
- added copper zone on F.Cu, net /PSU/FET_OUT
- added copper zone on B.Cu, net /TMC5160/BMA1
- added copper zone on F.Cu, net /TMC5160/BMA1
- added copper zone on B.Cu, net /TMC5160/BMA2
- added copper zone on F.Cu, net /TMC5160/BMA2
- added copper zone on B.Cu, net /TMC5160/BMB1
- added copper zone on F.Cu, net /TMC5160/BMB1
- added copper zone on B.Cu, net /TMC5160/BMB2
- added copper zone on F.Cu, net /TMC5160/BMB2
- added copper zone on F.Cu, net /TMC5160/SRA
- added copper zone on F.Cu, net /TMC5160/SRB
- added copper zone on F.Cu, net GND
- added copper zone on In1.Cu, net GND
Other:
- board size 80 x 100 mm -> 90 x 100 mm
- board text added: "A"
- board text added: "BOOT0"
- board text added: "DIR"
- board text added: "REF. SENSOR"
- board text added: "RESET"
- board text added: "SIG"
- board text added: "STEP"
- board text removed: "P"
